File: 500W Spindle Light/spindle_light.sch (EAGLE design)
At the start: 14 parts

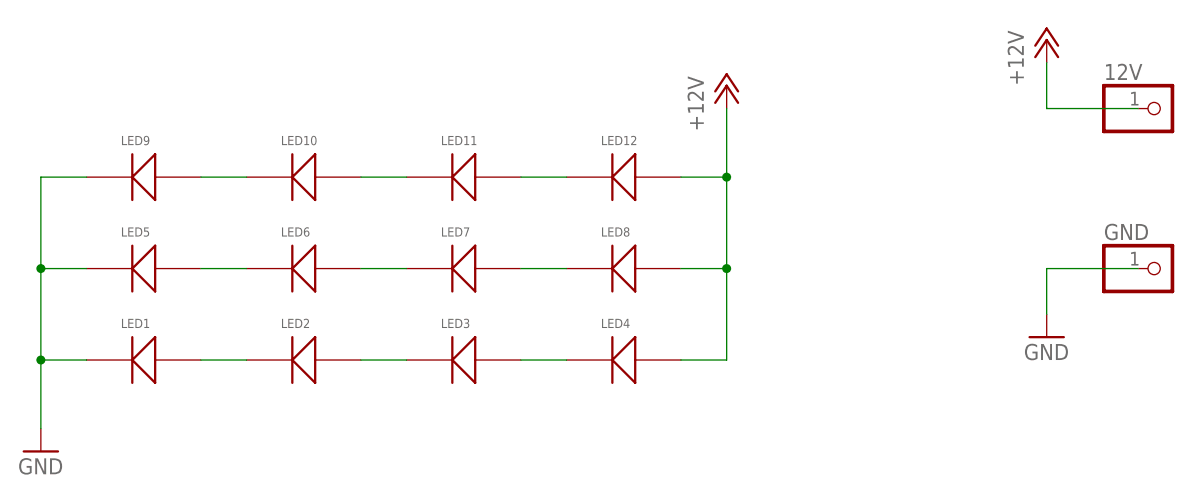
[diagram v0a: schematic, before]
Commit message: Smaller number of LEDs to make it a bit less bright
Everything connected and prototyped working fine so far. Need to check the dimensions
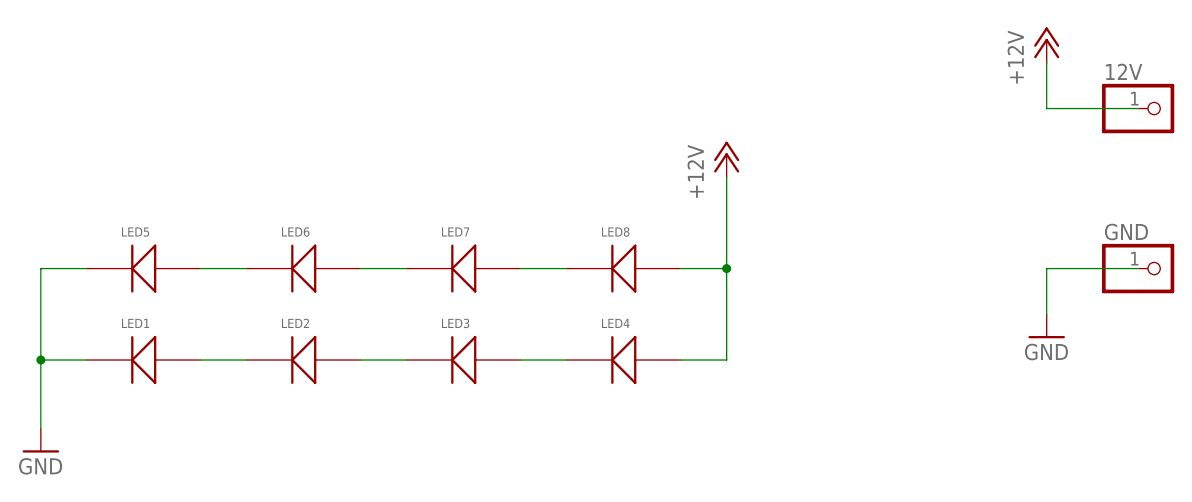
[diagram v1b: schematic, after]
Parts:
- removed LED10, LED11, LED12, LED9: RF-45HA50DS-EE-Y, NikodemBartnik:RF-45HA50DS-EE-Y
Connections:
- removed net N$1: LED10.P$2, LED9.P$1
- removed net N$6: LED10.P$1, LED11.P$2
- removed net N$7: LED11.P$1, LED12.P$2
- net +12V: no longer LED12.P$1
- net GND: no longer LED9.P$2
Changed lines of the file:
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@@
 <part name="LED7" library="NikodemBartnik" deviceset="RF-45HA50DS-EE-Y" device=""/>
 <part name="LED8" library="NikodemBartnik" deviceset="RF-45HA50DS-EE-Y" device=""/>
-<part name="LED9" library="NikodemBartnik" deviceset="RF-45HA50DS-EE-Y" device=""/>
 <part name="P+1" library="supply1" library_urn="urn:adsk.eagle:library:371" deviceset="+12V" device=""/>
 <part name="GND1" library="supply1" library_urn="urn:adsk.eagle:library:371" deviceset="GND" device=""/>
-<part name="LED10" library="NikodemBartnik" deviceset="RF-45HA50DS-EE-Y" device=""/>
-<part name="LED11" library="NikodemBartnik" deviceset="RF-45HA50DS-EE-Y" device=""/>
-<part name="LED12" library="NikodemBartnik" deviceset="RF-45HA50DS-EE-Y" device=""/>
 <part name="FRAME2" library="frames" library_urn="urn:adsk.eagle:library:229" deviceset="A4L-LOC" device=""/>
 <part name="12V" library="pinhead" library_urn="urn:adsk.eagle:library:325" deviceset="PINHD-1X1" device="" package3d_urn="urn:adsk.eagle:package:22485/2"/>
@@
 <attribute name="NAME" x="64.77" y="26.416" size="1.016" layer="95"/>
 </instance>
-<instance part="LED9" gate="G$1" x="15.24" y="33.02" smashed="yes">
-<attribute name="NAME" x="11.43" y="36.576" size="1.016" layer="95"/>
-</instance>
-<instance part="P+1" gate="1" x="78.74" y="43.18" smashed="yes">
-<attribute name="VALUE" x="76.2" y="38.1" size="1.778" layer="96" rot="R90"/>
+<instance part="P+1" gate="1" x="78.74" y="35.56" smashed="yes">
+<attribute name="VALUE" x="76.2" y="30.48" size="1.778" layer="96" rot="R90"/>
 </instance>
 <instance part="GND1" gate="1" x="2.54" y="2.54" smashed="yes">
 <attribute name="VALUE" x="0" y="0" size="1.778" layer="96"/>
-</instance>
-<instance part="LED10" gate="G$1" x="33.02" y="33.02" smashed="yes">
-<attribute name="NAME" x="29.21" y="36.576" size="1.016" layer="95"/>
-</instance>
-<instance part="LED11" gate="G$1" x="50.8" y="33.02" smashed="yes">
-<attribute name="NAME" x="46.99" y="36.576" size="1.016" layer="95"/>
-</instance>
-<instance part="LED12" gate="G$1" x="68.58" y="33.02" smashed="yes">
-<attribute name="NAME" x="64.77" y="36.576" size="1.016" layer="95"/>
 </instance>
 <instance part="FRAME2" gate="G$1" x="-81.28" y="-68.58" smashed="yes">
@@
 <wire x1="2.54" y1="12.7" x2="2.54" y2="22.86" width="0.1524" layer="91"/>
 <pinref part="LED1" gate="G$1" pin="P$2"/>
-<wire x1="2.54" y1="22.86" x2="2.54" y2="33.02" width="0.1524" layer="91"/>
 <wire x1="7.62" y1="12.7" x2="2.54" y2="12.7" width="0.1524" layer="91"/>
 <junction x="2.54" y="12.7"/>
-<pinref part="LED9" gate="G$1" pin="P$2"/>
-<wire x1="7.62" y1="33.02" x2="2.54" y2="33.02" width="0.1524" layer="91"/>
 <pinref part="LED5" gate="G$1" pin="P$2"/>
 <wire x1="7.62" y1="22.86" x2="2.54" y2="22.86" width="0.1524" layer="91"/>
-<junction x="2.54" y="22.86"/>
 </segment>
 <segment>
@@
 <pinref part="P+1" gate="1" pin="+12V"/>
 <wire x1="78.74" y1="12.7" x2="78.74" y2="22.86" width="0.1524" layer="91"/>
-<pinref part="LED12" gate="G$1" pin="P$1"/>
 <wire x1="78.74" y1="22.86" x2="78.74" y2="33.02" width="0.1524" layer="91"/>
-<wire x1="78.74" y1="33.02" x2="78.74" y2="40.64" width="0.1524" layer="91"/>
-<wire x1="73.66" y1="33.02" x2="78.74" y2="33.02" width="0.1524" layer="91"/>
-<junction x="78.74" y="33.02"/>
 <pinref part="LED8" gate="G$1" pin="P$1"/>
 <wire x1="73.66" y1="22.86" x2="78.74" y2="22.86" width="0.1524" layer="91"/>
@@
 <wire x1="124.46" y1="40.64" x2="114.3" y2="40.64" width="0.1524" layer="91"/>
 <wire x1="114.3" y1="40.64" x2="114.3" y2="45.72" width="0.1524" layer="91"/>
-</segment>
-</net>
-<net name="N$1" class="0">
-<segment>
-<pinref part="LED9" gate="G$1" pin="P$1"/>
-<pinref part="LED10" gate="G$1" pin="P$2"/>
-<wire x1="20.32" y1="33.02" x2="25.4" y2="33.02" width="0.1524" layer="91"/>
 </segment>
 </net>
@@
 </segment>
 </net>
-<net name="N$6" class="0">
-<segment>
-<pinref part="LED10" gate="G$1" pin="P$1"/>
-<pinref part="LED11" gate="G$1" pin="P$2"/>
-<wire x1="38.1" y1="33.02" x2="43.18" y2="33.02" width="0.1524" layer="91"/>
-</segment>
-</net>
-<net name="N$7" class="0">
-<segment>
-<pinref part="LED11" gate="G$1" pin="P$1"/>
-<pinref part="LED12" gate="G$1" pin="P$2"/>
-<wire x1="55.88" y1="33.02" x2="60.96" y2="33.02" width="0.1524" layer="91"/>
-</segment>
-</net>
